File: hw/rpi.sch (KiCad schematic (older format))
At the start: 6 parts

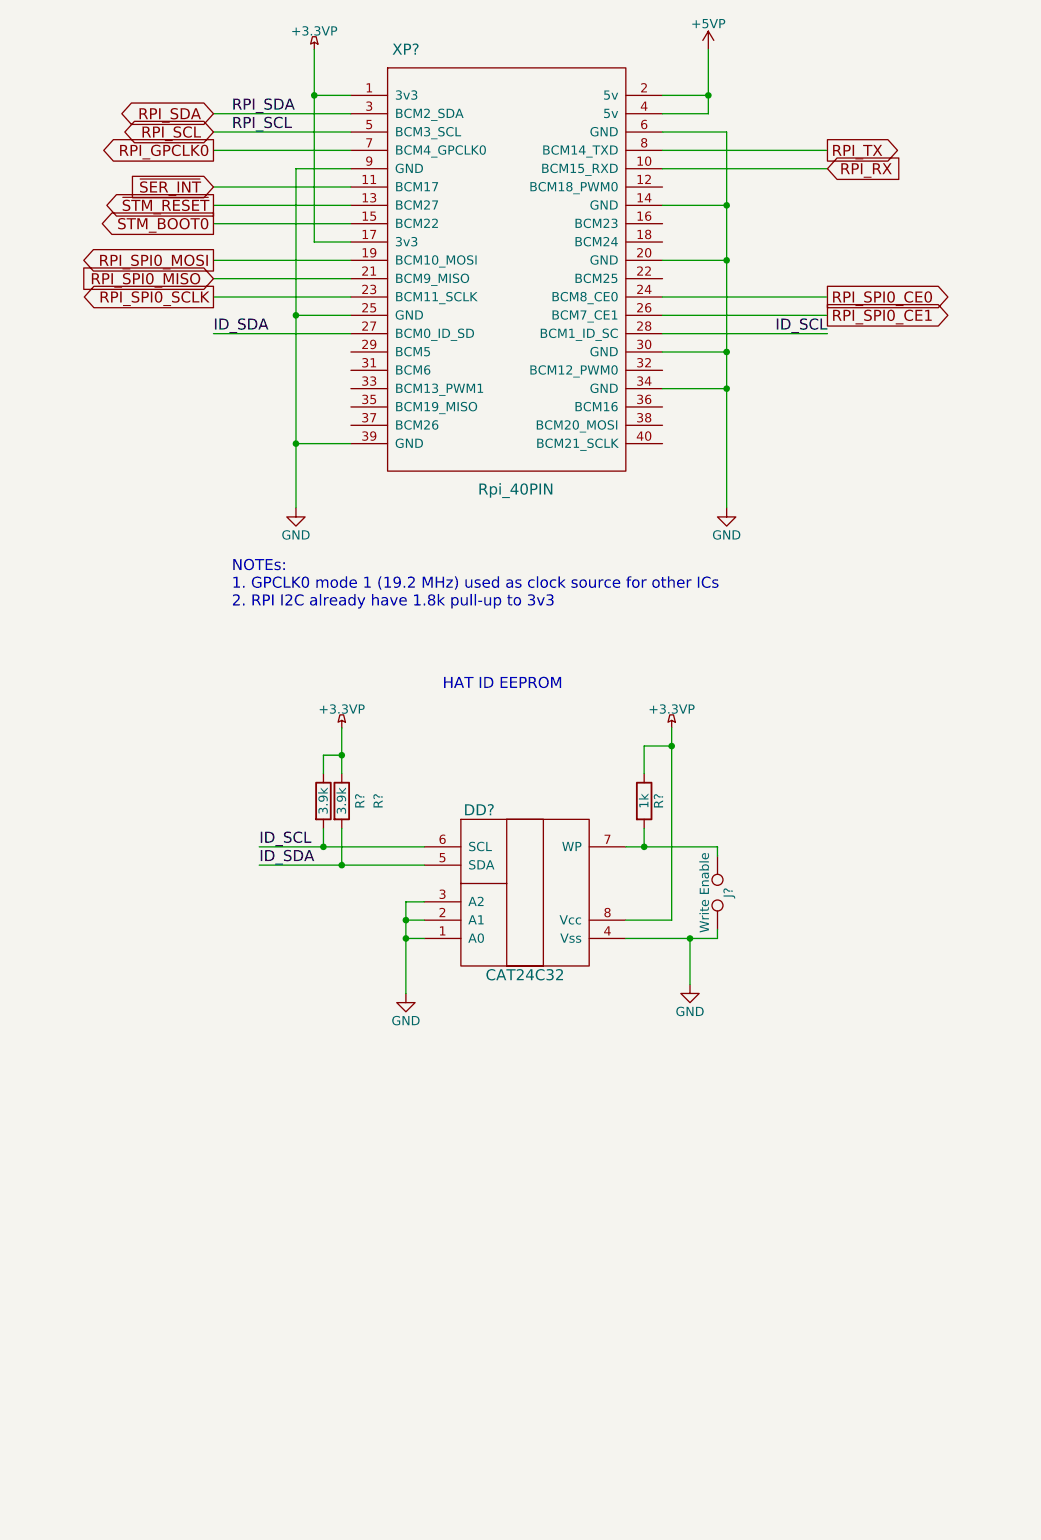
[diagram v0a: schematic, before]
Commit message: hw: add rpi hat zvd-circuit
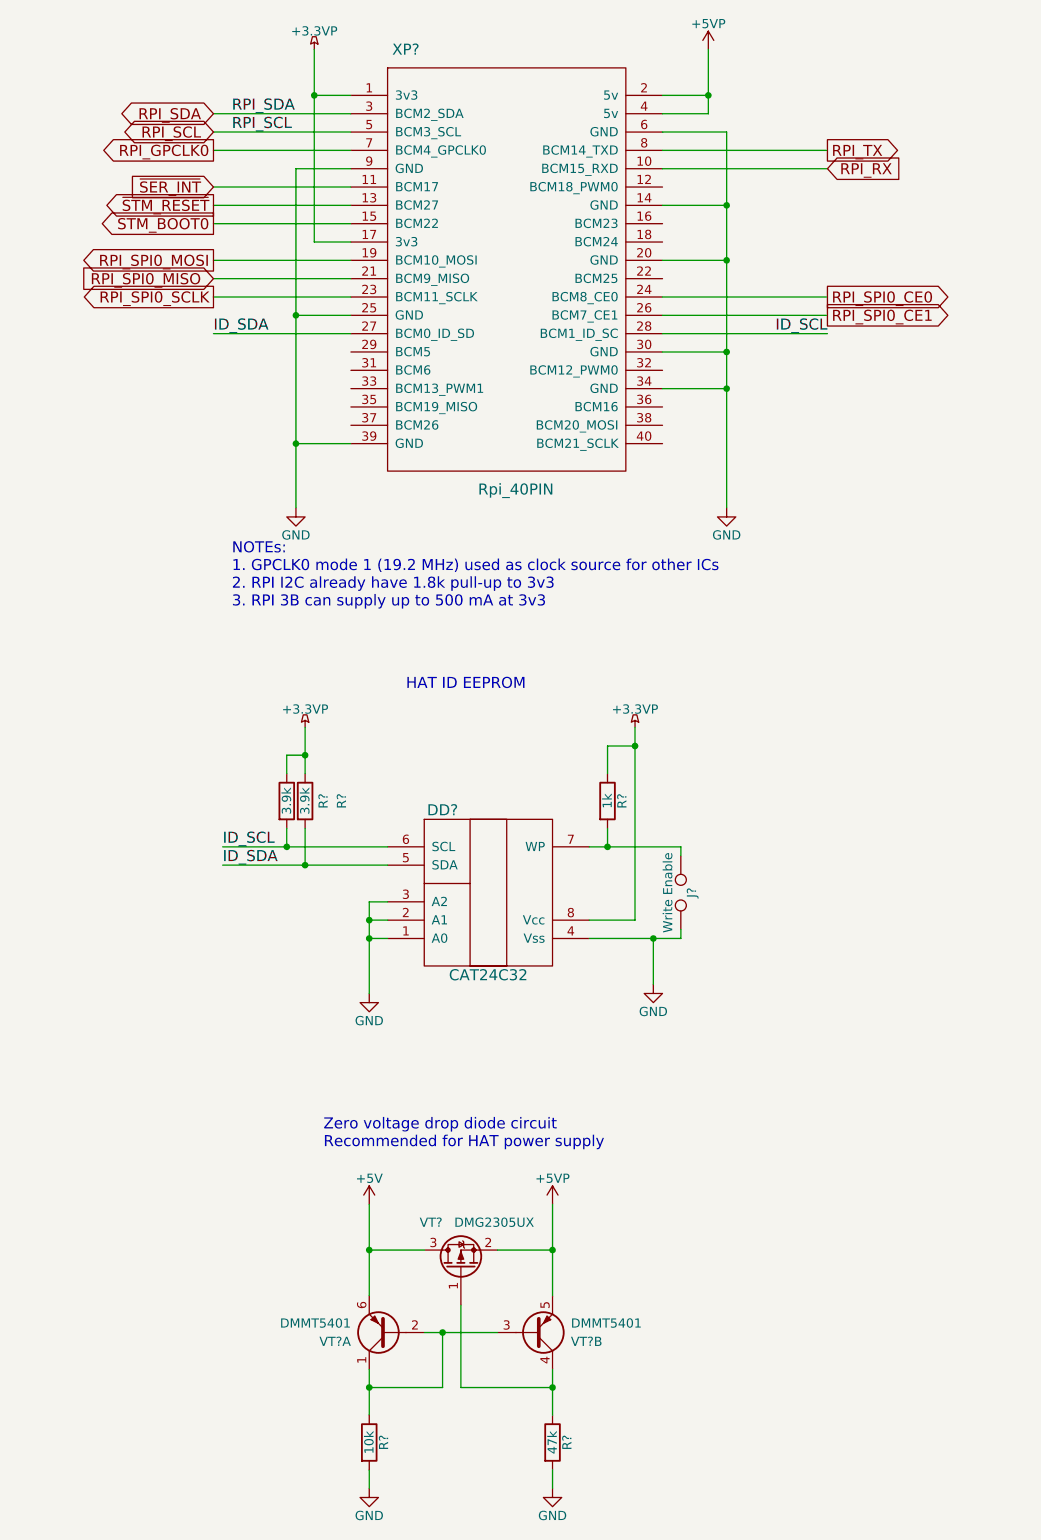
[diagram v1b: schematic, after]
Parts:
- added R?: 47k, symbol R
- added R?: 10k, symbol R
- added VT?: DMG2305UX, symbol DMG2305UX
- added VT? (x2): DMMT5401, symbol DMMT5401
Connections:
- net +5VP: now also VT?.2 (S), VT?.5 (E2)
- net GND: now also R?.2, R?.2
- new net: R?.1, VT?.1 (G), VT?.4 (C2)
- new net: R?.1, VT?.1 (C1), VT?.2 (B1), VT?.3 (B2)
- new net +5V: VT?.3 (D), VT?.6 (E1)
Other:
- note added: "NOTEs:\n1. GPCLK0 mode 1 (19.2 MHz) used as clock source for other ICs\n2. RPI I2C already have 1.8k pull-up to 3v3\n3. RPI 3B can supply up to 500 mA at 3v3"
- note added: "Zero voltage drop diode circuit\nRecommended for HAT power supply"
- note removed: "NOTEs:\n1. GPCLK0 mode 1 (19.2 MHz) used as clock source for other ICs\n2. RPI I2C already have 1.8k pull-up to 3v3"
- moved on the sheet: DD?, J?, R?

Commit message: hw: add MAX3109 symbol
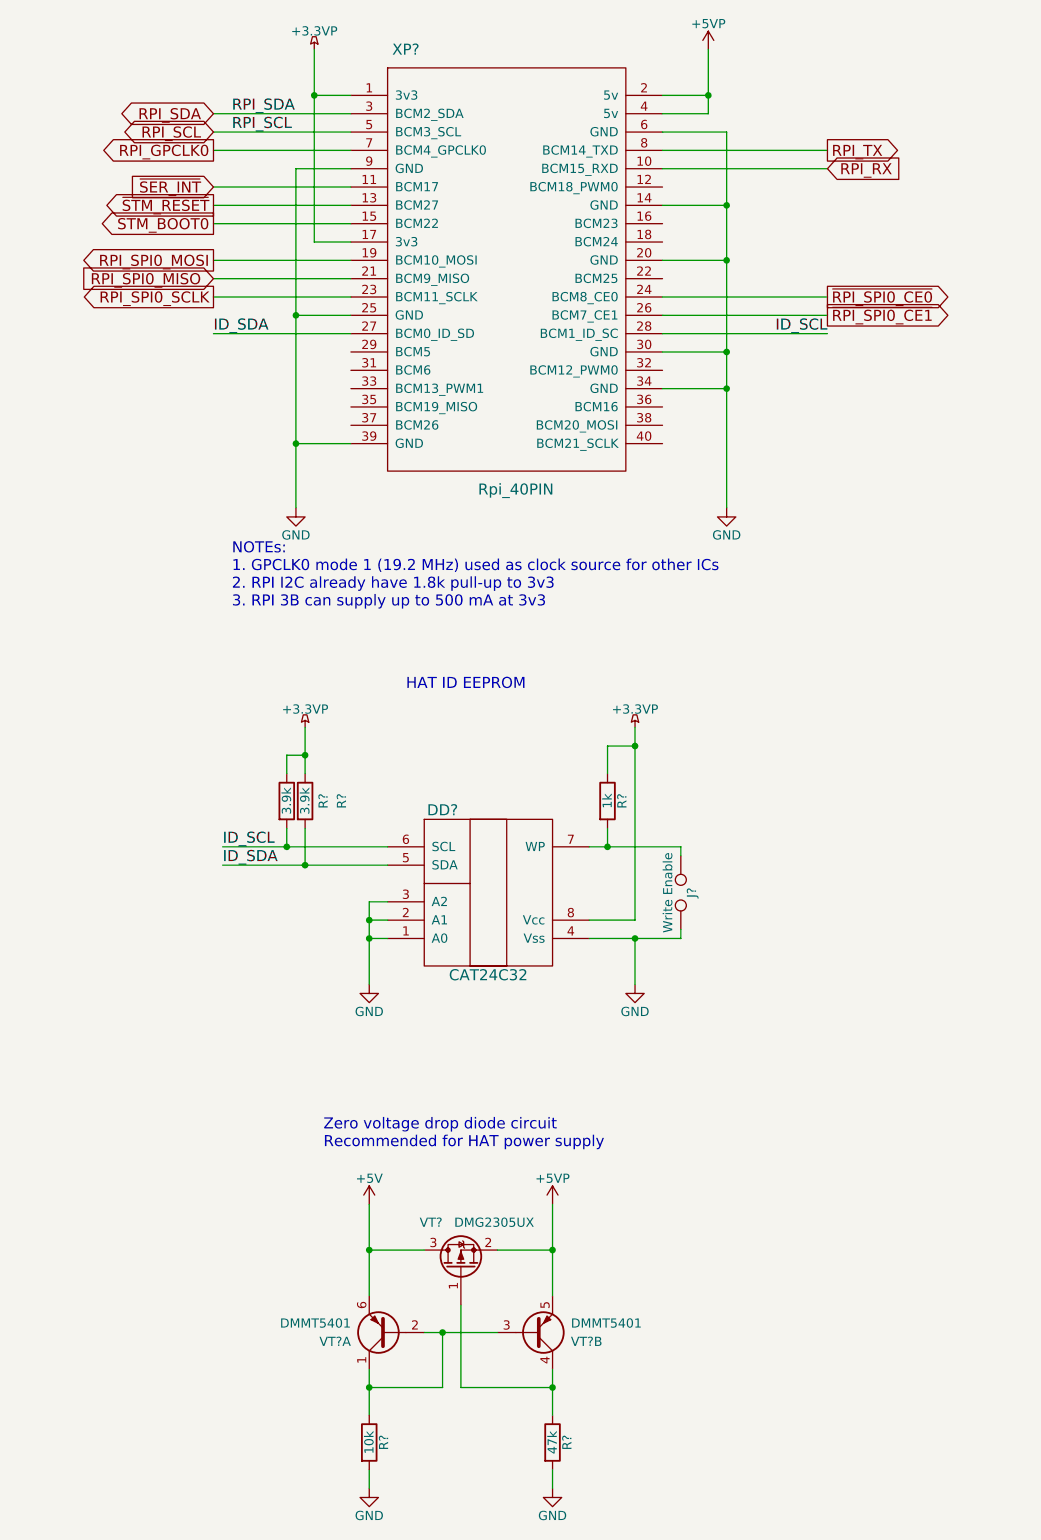
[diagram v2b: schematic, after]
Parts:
- VT?: footprint (none) -> TO_SOT_Packages_SMD:SOT-23_Handsoldering
- VT?: footprint (none) -> TO_SOT_Packages_SMD:SOT-23-6_Handsoldering
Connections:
- net RPI_SPI0_CE0 renamed ~RPI_SPI0_CE0
- net RPI_SPI0_CE1 renamed ~RPI_SPI0_CE1
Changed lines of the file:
@@
 RPI_SPI0_SCLK
 Text GLabel 6150 3050 2    60   Output ~ 0
-RPI_SPI0_CE0
+~RPI_SPI0_CE0
 Text GLabel 6150 3150 2    60   Output ~ 0
-RPI_SPI0_CE1
+~RPI_SPI0_CE1
 Wire Wire Line
 	5250 3050 6150 3050
@@
 L GND #PWR05
 U 1 1 5AB011CD
-P 5200 6800
-F 0 "#PWR05" H 5200 6550 50  0001 C CNN
-F 1 "GND" H 5200 6650 50  0000 C CNN
-F 2 "" H 5200 6800 50  0001 C CNN
-F 3 "" H 5200 6800 50  0001 C CNN
-	1    5200 6800
+P 5100 6800
+F 0 "#PWR05" H 5100 6550 50  0001 C CNN
+F 1 "GND" H 5100 6650 50  0000 C CNN
+F 2 "" H 5100 6800 50  0001 C CNN
+F 3 "" H 5100 6800 50  0001 C CNN
+	1    5100 6800
 	1    0    0    -1
 $EndComp
@@
 $EndComp
 Wire Wire Line
-	4850 6550 5200 6550
-Wire Wire Line
-	5200 6550 5350 6550
-Wire Wire Line
-	5200 6550 5200 6800
+	4850 6550 5100 6550
+Wire Wire Line
+	5100 6550 5350 6550
+Wire Wire Line
+	5100 6550 5100 6800
 Wire Wire Line
 	5100 6450 4850 6450
@@
 Wire Wire Line
 	5350 6550 5350 6500
-Connection ~ 5200 6550
+Connection ~ 5100 6550
 $Comp
 L GND #PWR08
 U 1 1 5AB0290A
-P 3650 6850
-F 0 "#PWR08" H 3650 6600 50  0001 C CNN
-F 1 "GND" H 3650 6700 50  0000 C CNN
-F 2 "" H 3650 6850 50  0001 C CNN
-F 3 "" H 3650 6850 50  0001 C CNN
-	1    3650 6850
+P 3650 6800
+F 0 "#PWR08" H 3650 6550 50  0001 C CNN
+F 1 "GND" H 3650 6650 50  0000 C CNN
+F 2 "" H 3650 6800 50  0001 C CNN
+F 3 "" H 3650 6800 50  0001 C CNN
+	1    3650 6800
 	1    0    0    -1
 $EndComp
@@
 	3650 6450 3650 6550
 Wire Wire Line
-	3650 6550 3650 6850
+	3650 6550 3650 6800
 Wire Wire Line
 	3750 6450 3650 6450
@@
 F 0 "VT?" V 4400 8450 50  0000 L CNN
 F 1 "DMG2305UX" V 4400 7950 50  0000 L CNN
-F 2 "" H 4350 8450 50  0001 C CNN
+F 2 "TO_SOT_Packages_SMD:SOT-23_Handsoldering" H 4350 8450 50  0001 C CNN
 F 3 "" H 4150 8350 50  0001 C CNN
 	1    4150 8350
@@
 Connection ~ 3650 9000
 $Comp
-L GND #PWR?
+L GND #PWR09
 U 1 1 5AB1380A
 P 4650 9550
-F 0 "#PWR?" H 4650 9300 50  0001 C CNN
+F 0 "#PWR09" H 4650 9300 50  0001 C CNN
 F 1 "GND" H 4650 9400 50  0000 C CNN
 F 2 "" H 4650 9550 50  0001 C CNN
@@
 Connection ~ 4050 8700
 $Comp
-L GND #PWR?
+L GND #PWR010
 U 1 1 5AB1428A
 P 3650 9550
-F 0 "#PWR?" H 3650 9300 50  0001 C CNN
+F 0 "#PWR010" H 3650 9300 50  0001 C CNN
 F 1 "GND" H 3650 9400 50  0000 C CNN
 F 2 "" H 3650 9550 50  0001 C CNN
@@
 F 0 "VT?" H 4750 8750 50  0000 L CNN
 F 1 "DMMT5401" H 4750 8650 50  0000 L CNN
-F 2 "" H 4750 8800 50  0001 C CNN
+F 2 "TO_SOT_Packages_SMD:SOT-23-6_Handsoldering" H 4750 8800 50  0001 C CNN
 F 3 "" H 4550 8700 50  0001 C CNN
 	2    4550 8700
@@
 $EndComp
 $Comp
-L +5VP #PWR?
+L +5VP #PWR011
 U 1 1 5AB14AE1
 P 4650 8000
-F 0 "#PWR?" H 4650 7850 50  0001 C CNN
+F 0 "#PWR011" H 4650 7850 50  0001 C CNN
 F 1 "+5VP" H 4650 8140 50  0000 C CNN
 F 2 "" H 4650 8000 50  0001 C CNN
@@
 	4650 8250 4650 8000
 $Comp
-L +5V #PWR?
+L +5V #PWR012
 U 1 1 5AB1599D
 P 3650 8000
-F 0 "#PWR?" H 3650 7850 50  0001 C CNN
+F 0 "#PWR012" H 3650 7850 50  0001 C CNN
 F 1 "+5V" H 3650 8140 50  0000 C CNN
 F 2 "" H 3650 8000 50  0001 C CNN

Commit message: hw: add uart conns
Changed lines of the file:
@@
 LIBS:rpi_con
 LIBS:ic
+LIBS:dronecode_con
 LIBS:obc-drone-hat-cache
 EELAYER 25 0
@@
 	3550 1950 3350 1950
 Wire Wire Line
-	3350 1700 3350 1950
-Wire Wire Line
-	3350 1950 3350 2750
+	3350 1700 3350 2750
 Wire Wire Line
 	3350 2750 3550 2750
@@
 	3550 2350 3250 2350
 Wire Wire Line
-	3250 2350 3250 3150
-Wire Wire Line
-	3250 3150 3250 3850
-Wire Wire Line
-	3250 3850 3250 4200
+	3250 2350 3250 4200
 Wire Wire Line
 	3550 3150 3250 3150
@@
 	5500 2050 5250 2050
 Wire Wire Line
-	5500 1700 5500 1950
-Wire Wire Line
-	5500 1950 5500 2050
+	5500 1700 5500 2050
 Wire Wire Line
 	5250 1950 5500 1950
@@
 	5250 2150 5600 2150
 Wire Wire Line
-	5600 2150 5600 2550
-Wire Wire Line
-	5600 2550 5600 2850
-Wire Wire Line
-	5600 2850 5600 3350
-Wire Wire Line
-	5600 3350 5600 3550
-Wire Wire Line
-	5600 3550 5600 4200
+	5600 2150 5600 4200
 Wire Wire Line
 	5250 2550 5600 2550
@@
 $EndComp
 Wire Wire Line
-	4850 6550 5100 6550
-Wire Wire Line
-	5100 6550 5350 6550
+	4850 6550 5350 6550
 Wire Wire Line
 	5100 6550 5100 6800
@@
 	5100 6450 4850 6450
 Wire Wire Line
-	5100 5400 5100 5500
-Wire Wire Line
-	5100 5500 5100 6450
+	5100 5400 5100 6450
 $Comp
 L R R?
@@
 $EndComp
 Wire Wire Line
-	4850 6050 4950 6050
-Wire Wire Line
-	4950 6050 5350 6050
+	4850 6050 5350 6050
 Wire Wire Line
 	4950 6050 4950 5950
@@
 Connection ~ 5100 5500
 Wire Wire Line
-	2850 6050 3200 6050
-Wire Wire Line
-	3200 6050 3750 6050
-Wire Wire Line
-	2850 6150 3300 6150
-Wire Wire Line
-	3300 6150 3750 6150
+	2850 6050 3750 6050
+Wire Wire Line
+	2850 6150 3750 6150
 $Comp
 L R R?
@@
 Connection ~ 3300 6150
 Wire Wire Line
-	3300 5400 3300 5550
-Wire Wire Line
-	3300 5550 3300 5650
+	3300 5400 3300 5650
 Wire Wire Line
 	3200 5650 3200 5550
@@
 	3750 6350 3650 6350
 Wire Wire Line
-	3650 6350 3650 6450
-Wire Wire Line
-	3650 6450 3650 6550
-Wire Wire Line
-	3650 6550 3650 6800
+	3650 6350 3650 6800
 Wire Wire Line
 	3750 6450 3650 6450
@@
 $EndComp
 Wire Wire Line
-	3650 8250 3650 8250
-Wire Wire Line
 	3650 8250 3950 8250
 Wire Wire Line
 	4350 8250 4650 8250
 Wire Wire Line
-	4650 8250 4650 8250
-Wire Wire Line
-	4650 8500 4650 8250
+	4650 8000 4650 8500
 Connection ~ 4650 8250
 Wire Wire Line
-	3650 8500 3650 8250
+	3650 8000 3650 8500
 Connection ~ 3650 8250
 Wire Wire Line
-	3650 8900 3650 9000
-Wire Wire Line
-	3650 9000 3650 9150
+	3650 8900 3650 9150
 Connection ~ 3650 9000
 $Comp
@@
 $EndComp
 Wire Wire Line
-	4650 8900 4650 9000
-Wire Wire Line
-	4650 9000 4650 9150
+	4650 8900 4650 9150
 Wire Wire Line
 	4150 8550 4150 9000
@@
 Connection ~ 4650 9000
 Wire Wire Line
-	3950 8700 4050 8700
-Wire Wire Line
-	4050 8700 4350 8700
+	3950 8700 4350 8700
 Wire Wire Line
 	4050 8700 4050 9000
@@
 	1    0    0    -1
 $EndComp
-Wire Wire Line
-	4650 8250 4650 8000
 $Comp
 L +5V #PWR012
@@
 	1    0    0    -1
 $EndComp
-Wire Wire Line
-	3650 8000 3650 8250
 Text Notes 3400 7700 0    60   ~ 0
 Zero voltage drop diode circuit\nRecommended for HAT power supply

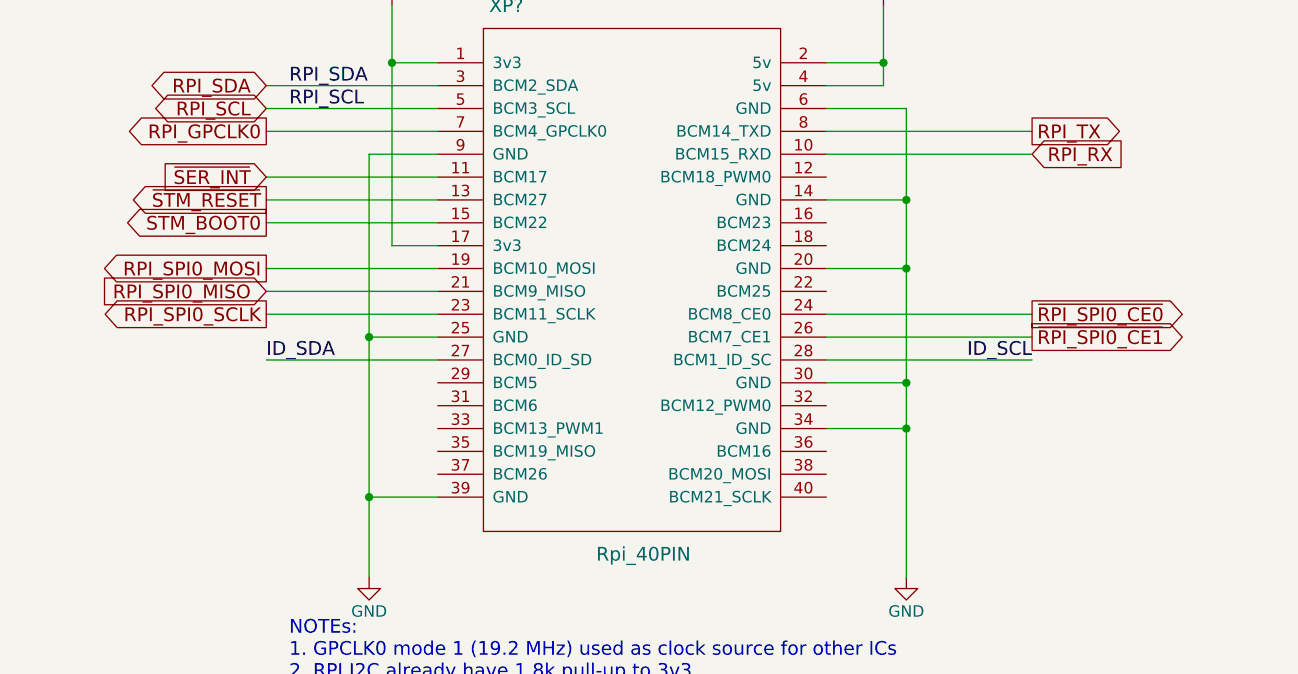
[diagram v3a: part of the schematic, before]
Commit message: hw: add conn and dc-dc sheets
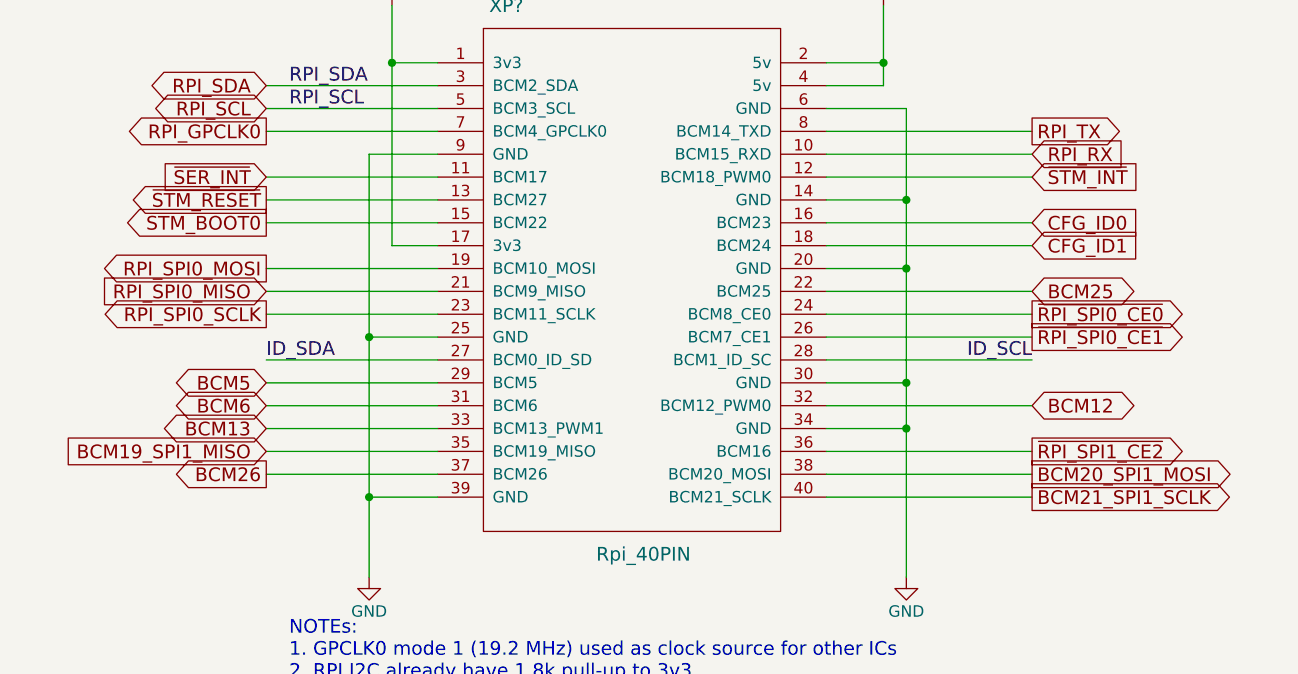
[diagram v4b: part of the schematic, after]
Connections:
- net ~STM_INT: now reaches XP?.12 (BCM18_PWM0)
- net CFG_ID0: now reaches XP?.16 (BCM23)
- net CFG_ID1: now reaches XP?.18 (BCM24)
- net BCM25: now reaches XP?.22 (BCM25)
- net BCM5: now reaches XP?.29 (BCM5)
- net BCM6: now reaches XP?.31 (BCM6)
- net BCM12: now reaches XP?.32 (BCM12_PWM0)
- net BCM13: now reaches XP?.33 (BCM13_PWM1)
- net BCM19_SPI1_MISO: now reaches XP?.35 (BCM19_MISO)
- net ~RPI_SPI1_CE2: now reaches XP?.36 (BCM16)
- net BCM26: now reaches XP?.37 (BCM26)
- net BCM20_SPI1_MOSI: now reaches XP?.38 (BCM20_MOSI)
- net BCM21_SPI1_SCLK: now reaches XP?.40 (BCM21_SCLK)
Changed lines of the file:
@@
 $Descr A4 8268 11693 portrait
 encoding utf-8
-Sheet 2 5
+Sheet 2 7
 Title "OBC Drone Hat"
 Date "2018-03-19"
@@
 Text Notes 3400 7700 0    60   ~ 0
 Zero voltage drop diode circuit\nRecommended for HAT power supply
+Text GLabel 6150 2450 2    60   Input ~ 0
+~STM_INT
+Wire Wire Line
+	6150 2450 5250 2450
+Text GLabel 6150 3750 2    60   Output ~ 0
+BCM20_SPI1_MOSI
+Text GLabel 6150 3850 2    60   Output ~ 0
+BCM21_SPI1_SCLK
+Text GLabel 6150 3650 2    60   Output ~ 0
+~RPI_SPI1_CE2
+Text GLabel 2800 3650 0    60   Input ~ 0
+BCM19_SPI1_MISO
+Wire Wire Line
+	5250 3650 6150 3650
+Wire Wire Line
+	5250 3750 6150 3750
+Wire Wire Line
+	5250 3850 6150 3850
+Wire Wire Line
+	2800 3650 3550 3650
+Text GLabel 6150 2650 2    60   Input ~ 0
+CFG_ID0
+Text GLabel 6150 2750 2    60   Input ~ 0
+CFG_ID1
+Wire Wire Line
+	6150 2650 5250 2650
+Wire Wire Line
+	6150 2750 5250 2750
+Text GLabel 2800 3750 0    60   Output ~ 0
+BCM26
+Text GLabel 2800 3550 0    60   BiDi ~ 0
+BCM13
+Wire Wire Line
+	3550 3550 2800 3550
+Wire Wire Line
+	2800 3750 3550 3750
+Text GLabel 2800 3350 0    60   BiDi ~ 0
+BCM5
+Text GLabel 2800 3450 0    60   BiDi ~ 0
+BCM6
+Wire Wire Line
+	2800 3350 3550 3350
+Wire Wire Line
+	3550 3450 2800 3450
+Text GLabel 6150 3450 2    60   BiDi ~ 0
+BCM12
+Text GLabel 6150 2950 2    60   BiDi ~ 0
+BCM25
+Wire Wire Line
+	6150 2950 5250 2950
+Wire Wire Line
+	5250 3450 6150 3450
 $EndSCHEMATC
